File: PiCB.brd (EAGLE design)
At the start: 81.3 x 63.5 mm, 30 parts

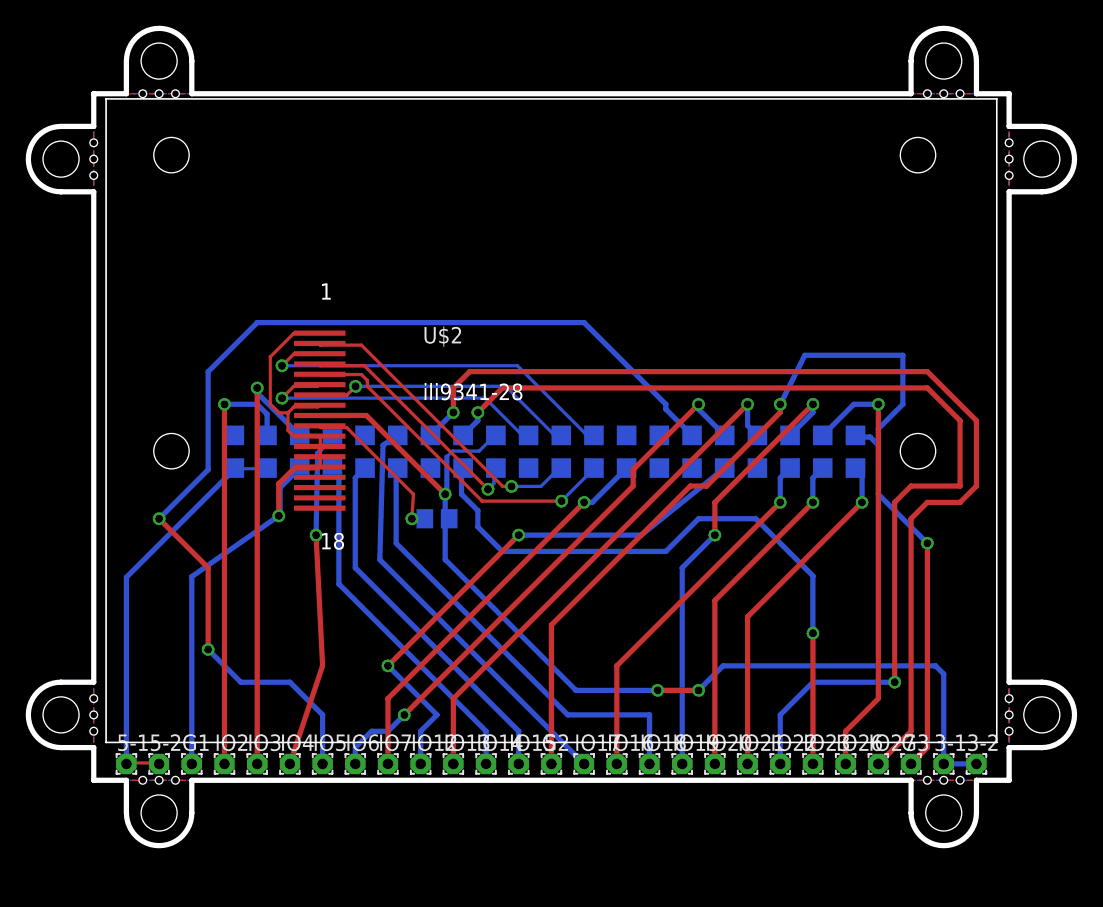
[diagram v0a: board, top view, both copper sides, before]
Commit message: Add files via upload
made the gpio on 2 rows, added more grounds and better spacing
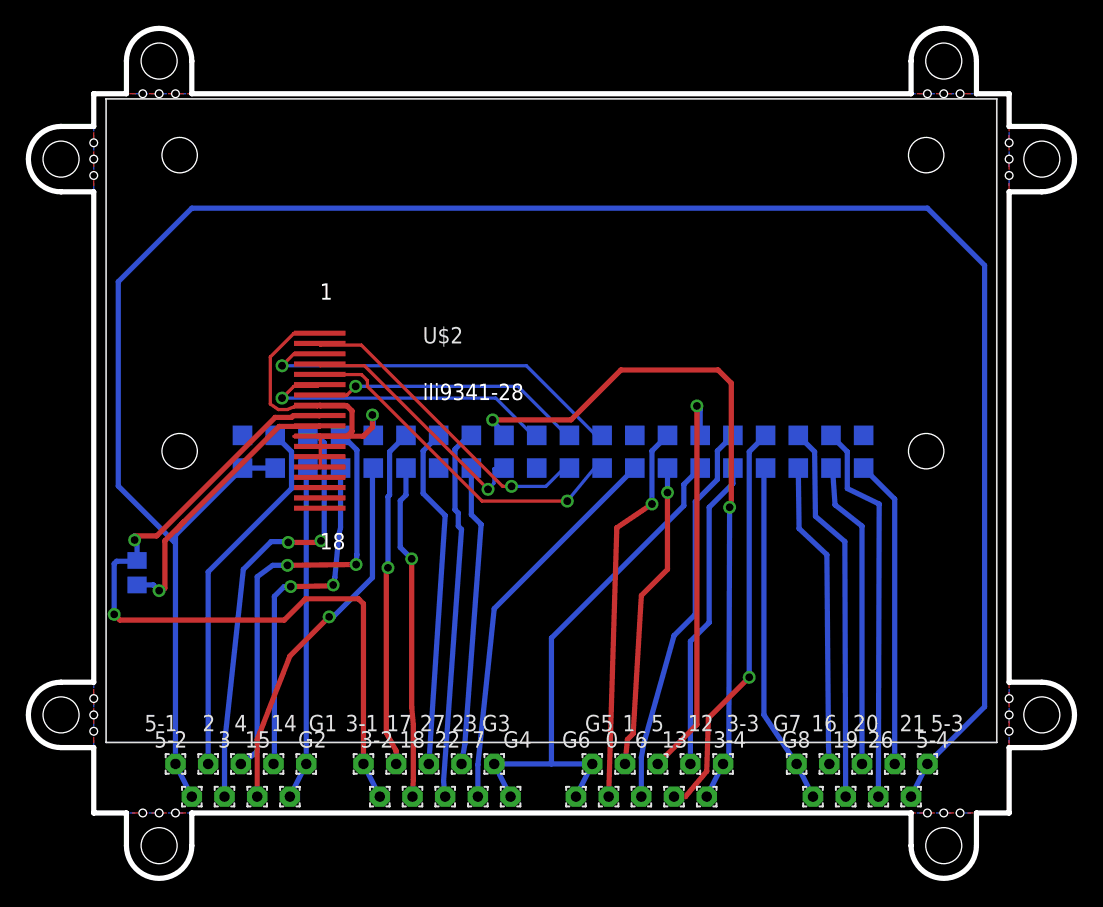
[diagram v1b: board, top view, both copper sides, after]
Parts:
- removed IO12, IO13, IO14, IO15, IO16, IO17, IO18, IO19, IO2, IO20, IO21, IO22, IO23, IO26, IO27, IO3, IO4, IO5, IO6, IO7: (no value), wirepad:1,6/0,8
- added 0, 1, 12, 13, 14, 15, 16, 17, 18, 19, 2, 20, 21, 22, 23, 26, 27, 3, 3-3, 3-4, 4, 5, 5-3, 5-4, 6, 7, G4, G5, G6, G7, G8: (no value), wirepad:1,6/0,8
- moved 3-2 46.4 mm to (22.2, 1.27)
- moved 3-1 45.1 mm to (21.0, 3.81)
- moved G3 32.4 mm to (31.1, 3.81)
- moved R1 23.7 mm to (3.37, 18.7), turned to 90 degrees
- moved G2 20.5 mm to (15.2, 1.27)
- moved G1 8.89 mm to (16.5, 3.81)
- moved 5-1 3.81 mm to (6.35, 3.81)
- moved 5-2 3.59 mm to (7.62, 1.27)
- moved PI1 0.63 mm to (3.17, 54.6)
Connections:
- new net N$31: 0.1, PI1.27
- new net N$32: 1.1, PI1.28
- net 5V0@2: now also 5-3.1, 5-4.1
- net GND: now also G4.1, G5.1, G6.1, G7.1, G8.1
- net N$10: now also 13.1; no longer IO13.1
- net N$11: now also 6.1; no longer IO6.1
- net N$12: now also 5.1; no longer IO5.1
- net N$13: now also 21.1; no longer IO21.1
- net N$14: now also 20.1; no longer IO20.1
- net N$15: now also 16.1; no longer IO16.1
- net N$16: now also 12.1; no longer IO12.1
- net N$17: now also 7.1; no longer IO7.1
- net N$18: now also 14.1; no longer IO14.1
- net N$19: now also 3-3.1, 3-4.1
- net N$20: now also 23.1; no longer IO23.1
- net N$21: now also 18.1; no longer IO18.1
- net N$22: now also 15.1; no longer IO15.1
- net N$23: now also 22.1; no longer IO22.1
- net N$24: now also 4.1; no longer IO4.1
- net N$25: now also 27.1; no longer IO27.1
- net N$26: now also 17.1; no longer IO17.1
- net N$27: now also 3.1; no longer IO3.1
- net N$28: now also 2.1; no longer IO2.1
- net N$8: now also 26.1; no longer IO26.1
- net N$9: now also 19.1; no longer IO19.1
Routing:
- net 5V0@2: track 31.6 -> 167.6 mm
- net N$25: track 78.5 -> 26.8 mm, vias 1 -> 0
- net N$12: track 82.6 -> 31.5 mm, vias 2 -> 1
- net N$23: track 80.0 -> 29.0 mm, vias 2 -> 0
- net GND: track 130.0 -> 86.7 mm, vias 3 -> 0
- net N$19: track 78.6 -> 116.5 mm, vias 3 -> 4
- net N$31: track 0.00 -> 30.0 mm, vias 0 -> 1
- net N$20: track 49.5 -> 23.4 mm, vias 1 -> 0
- net N$32: track 0.00 -> 24.0 mm, vias 0 -> 1
- net GND@7: track 4.31 -> 27.8 mm
- net N$16: track 41.9 -> 24.4 mm, vias 2 -> 0
- net N$11: track 43.0 -> 30.3 mm, vias 2 -> 0
- net N$5: track 12.4 -> 22.7 mm
- net N$21: track 34.9 -> 26.1 mm, vias 0 -> 1
- net N$10: track 40.1 -> 31.4 mm
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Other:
- board size 81.3 x 63.5 mm -> 81.3 x 66 mm

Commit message: Add files via upload
straightened out some traces and moved the gpio silkscreen to the back so it doesnt get covered
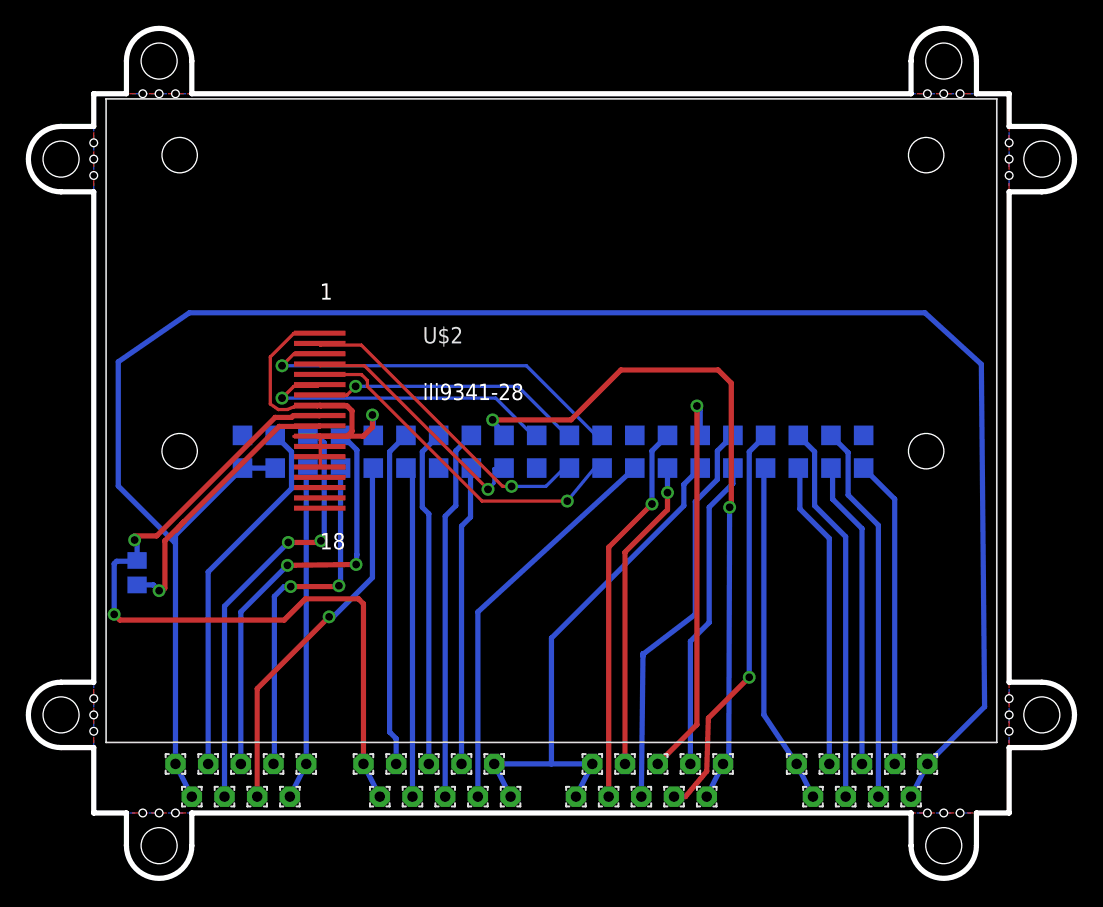
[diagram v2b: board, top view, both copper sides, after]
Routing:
- net 5V0@2: track 167.6 -> 152.0 mm
- net N$11: track 30.3 -> 31.3 mm
- net N$24: track 33.8 -> 32.9 mm
- net N$17: track 30.1 -> 30.9 mm
- net N$22: track 28.9 -> 29.4 mm
- net N$8: track 30.1 -> 29.6 mm
- net N$25: track 26.8 -> 26.3 mm
- net N$21: track 26.1 -> 25.7 mm, vias 1 -> 0
- net N$26: track 26.4 -> 26.3 mm, vias 1 -> 0
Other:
- board text added: "3.3v"
- board text added: "5v"
- board text added: "gnd"
